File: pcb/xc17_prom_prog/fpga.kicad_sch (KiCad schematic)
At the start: 18 parts, among them J3 Conn_02x20_Odd_Even, U3 ICE40HX1K-VQ100

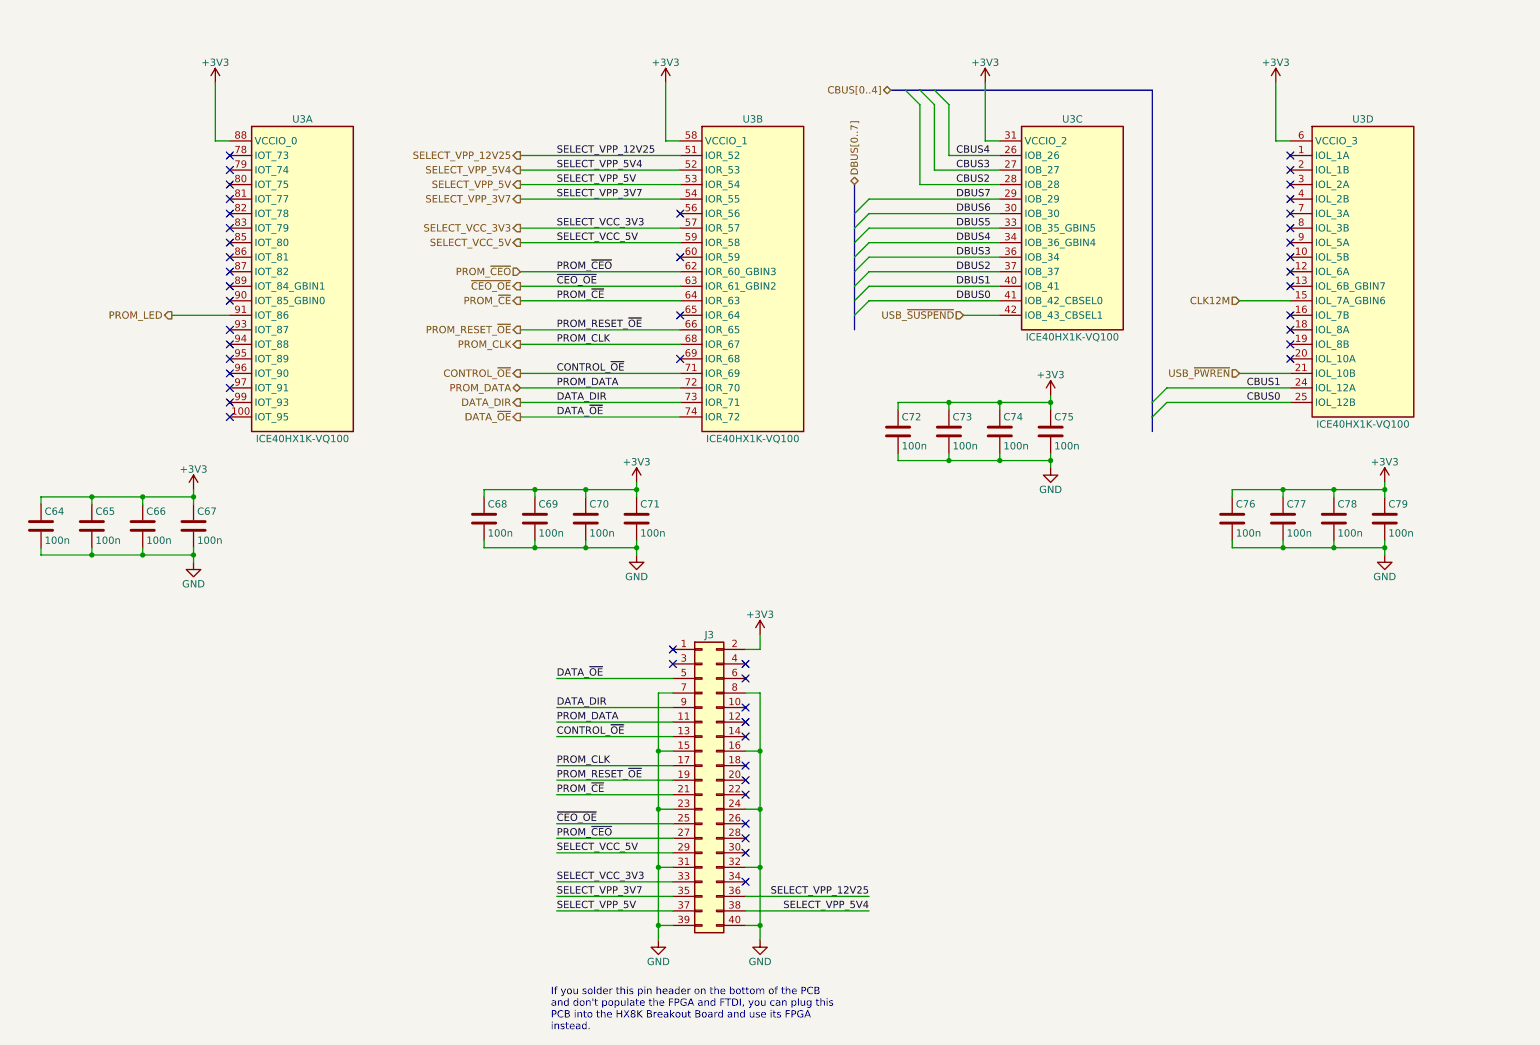
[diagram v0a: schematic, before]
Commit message: Fix MOSFETs
 * Block MOSFET body diodes by placing two MOSFETs in anti series.
 * Connect PROM LED to pin header.
 * Add transistors to actively pull PROM VCC and VPP low.
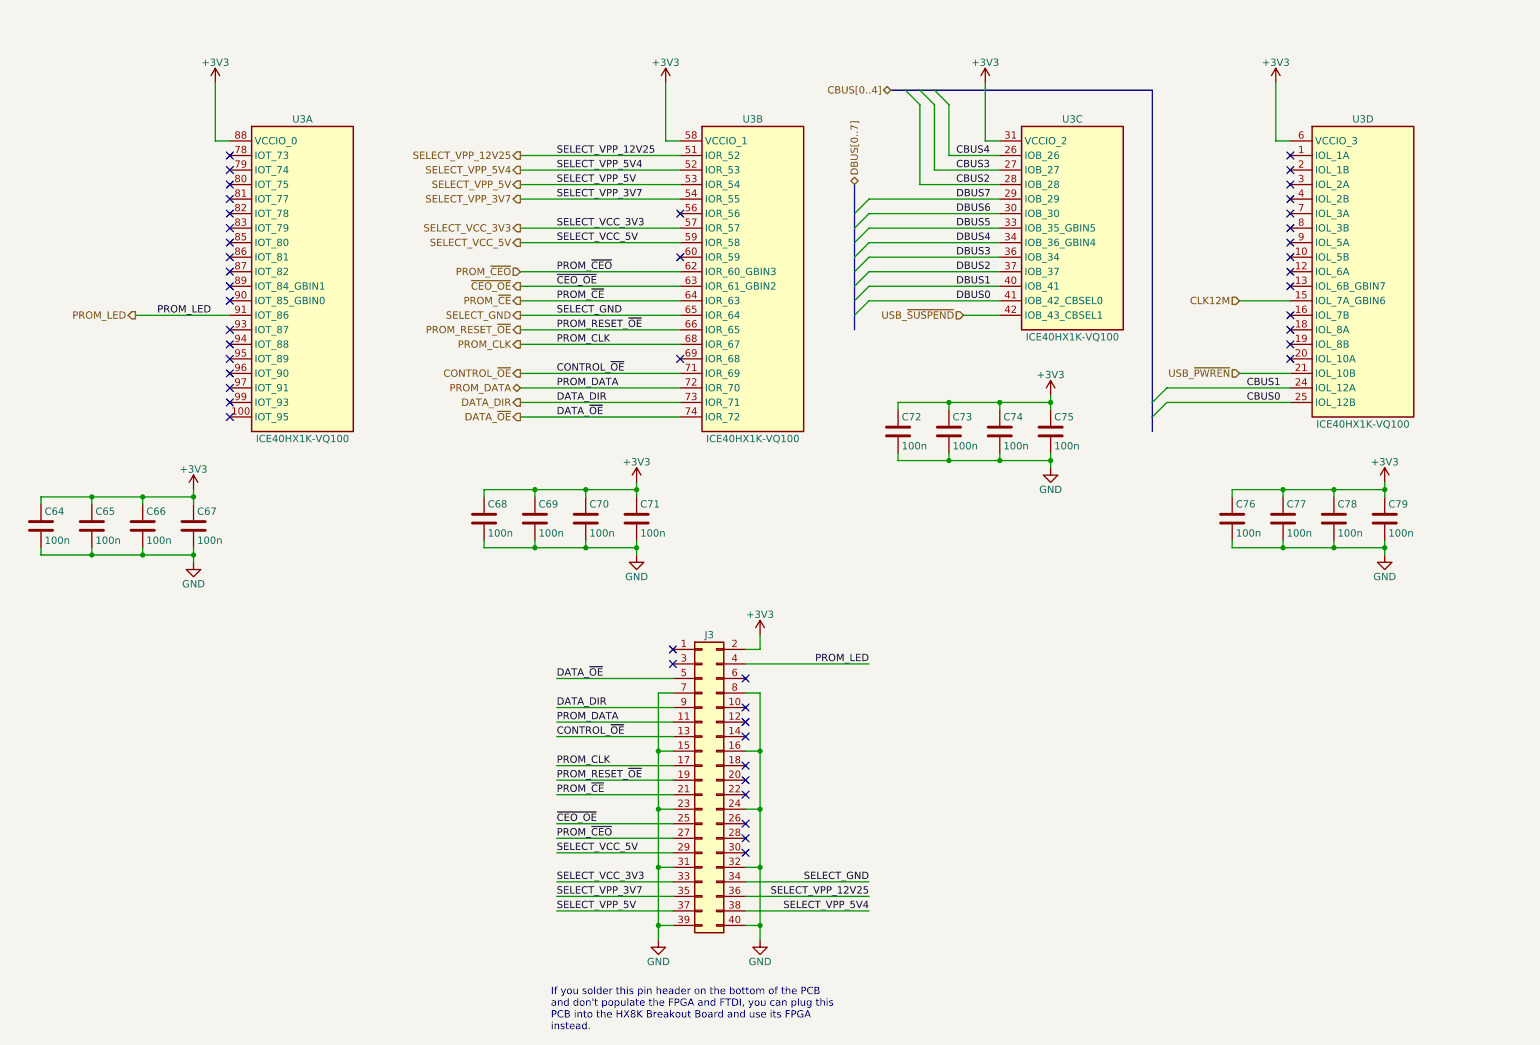
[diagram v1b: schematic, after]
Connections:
- net PROM_LED: now also J3.4 (Pin_4)
- net SELECT_GND: now reaches U3.65 (IOR_64)
- net SELECT_GND: now also J3.34 (Pin_34)
- no-connect marks 50 -> 47
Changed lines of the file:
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@@
 	(title_block
 		(title "XC17xxx PROM Programmer")
-		(date "2024-11-02")
-		(rev "0")
+		(date "2024-11-23")
+		(rev "1")
 		(company "CC-BY-SA-4.0 Michael Singer")
 		(comment 1 "https://github.com/msinger/xc17_prom_prog/")
@@
 	)
 	(no_connect
-		(at 144.78 167.64)
-	)
-	(no_connect
 		(at 144.78 137.16)
 	)
@@
 	)
 	(no_connect
-		(at 133.35 68.58)
-	)
-	(no_connect
 		(at 144.78 142.24)
 	)
 	(no_connect
-		(at 144.78 129.54)
-	)
-	(no_connect
 		(at 240.03 55.88)
 	)
@@
 	(wire
 		(pts
+			(xy 144.78 129.54) (xy 166.37 129.54)
+		)
+		(stroke
+			(width 0)
+			(type default)
+		)
+	)
+	(wire
+		(pts
 			(xy 99.06 107.95) (xy 99.06 109.22)
 		)
@@
 	(wire
 		(pts
-			(xy 44.45 68.58) (xy 54.61 68.58)
+			(xy 38.1 68.58) (xy 54.61 68.58)
 		)
 		(stroke
@@
 	(wire
 		(pts
+			(xy 105.41 68.58) (xy 133.35 68.58)
+		)
+		(stroke
+			(width 0)
+			(type default)
+		)
+	)
+	(wire
+		(pts
 			(xy 132.08 165.1) (xy 129.54 165.1)
 		)
@@
 	(wire
 		(pts
+			(xy 144.78 167.64) (xy 166.37 167.64)
+		)
+		(stroke
+			(width 0)
+			(type default)
+		)
+	)
+	(wire
+		(pts
 			(xy 99.06 109.22) (xy 107.95 109.22)
 		)
@@
 		)
 	)
+	(label "PROM_LED"
+		(at 41.91 68.58 0)
+		(fields_autoplaced yes)
+		(effects
+			(font
+				(size 1.27 1.27)
+			)
+			(justify left bottom)
+		)
+	)
 	(label "DATA_DIR"
 		(at 111.76 83.82 0)
@@
 		)
 	)
+	(label "SELECT_GND"
+		(at 166.37 167.64 180)
+		(fields_autoplaced yes)
+		(effects
+			(font
+				(size 1.27 1.27)
+			)
+			(justify right bottom)
+		)
+	)
 	(label "SELECT_VCC_3V3"
 		(at 111.76 167.64 0)
@@
 		)
 	)
+	(label "PROM_LED"
+		(at 166.37 129.54 180)
+		(fields_autoplaced yes)
+		(effects
+			(font
+				(size 1.27 1.27)
+			)
+			(justify right bottom)
+		)
+	)
 	(label "PROM_RESET_~{OE}"
 		(at 111.76 71.12 0)
@@
 		)
 	)
+	(label "SELECT_GND"
+		(at 111.76 68.58 0)
+		(fields_autoplaced yes)
+		(effects
+			(font
+				(size 1.27 1.27)
+			)
+			(justify left bottom)
+		)
+	)
 	(label "PROM_CLK"
 		(at 111.76 73.66 0)
@@
 		)
 	)
+	(hierarchical_label "SELECT_GND"
+		(shape output)
+		(at 105.41 68.58 180)
+		(fields_autoplaced yes)
+		(effects
+			(font
+				(size 1.27 1.27)
+			)
+			(justify right)
+		)
+	)
 	(hierarchical_label "SELECT_VCC_5V"
 		(shape output)
@@
 	(hierarchical_label "PROM_LED"
 		(shape output)
-		(at 44.45 68.58 180)
+		(at 38.1 68.58 180)
 		(fields_autoplaced yes)
 		(effects
@@
 		(on_board yes)
 		(dnp no)
-		(property "Reference" "#PWR0106"
+		(property "Reference" "#PWR0110"
 			(at 198.12 86.36 0)
 			(effects
@@
 			(project "xc17_prom_prog"
 				(path "/3afea672-343d-4fc8-b012-067ac21cc0e9/a8f52001-7a25-4283-bdf4-2dead0af6825"
-					(reference "#PWR0106")
+					(reference "#PWR0110")
 					(unit 1)
 				)
@@
 		(on_board yes)
 		(dnp no)
-		(property "Reference" "#PWR099"
+		(property "Reference" "#PWR0103"
 			(at 125.73 101.6 0)
 			(effects
@@
 			(project "xc17_prom_prog"
 				(path "/3afea672-343d-4fc8-b012-067ac21cc0e9/a8f52001-7a25-4283-bdf4-2dead0af6825"
-					(reference "#PWR099")
+					(reference "#PWR0103")
 					(unit 1)
 				)
@@
 		(on_board yes)
 		(dnp no)
-		(property "Reference" "#PWR097"
+		(property "Reference" "#PWR0101"
 			(at 48.26 118.11 0)
 			(effects
@@
 			(project "xc17_prom_prog"
 				(path "/3afea672-343d-4fc8-b012-067ac21cc0e9/a8f52001-7a25-4283-bdf4-2dead0af6825"
-					(reference "#PWR097")
+					(reference "#PWR0101")
 					(unit 1)
 				)
@@
 		(on_board yes)
 		(dnp no)
-		(property "Reference" "#PWR0104"
+		(property "Reference" "#PWR0108"
 			(at 147.32 184.15 0)
 			(effects
@@
 			(project ""
 				(path "/3afea672-343d-4fc8-b012-067ac21cc0e9/a8f52001-7a25-4283-bdf4-2dead0af6825"
-					(reference "#PWR0104")
+					(reference "#PWR0108")
 					(unit 1)
 				)
@@
 		(on_board yes)
 		(dnp no)
-		(property "Reference" "#PWR098"
+		(property "Reference" "#PWR0102"
 			(at 52.07 31.75 0)
 			(effects
@@
 			(project "xc17_prom_prog"
 				(path "/3afea672-343d-4fc8-b012-067ac21cc0e9/a8f52001-7a25-4283-bdf4-2dead0af6825"
-					(reference "#PWR098")
+					(reference "#PWR0102")
 					(unit 1)
 				)
@@
 		(on_board yes)
 		(dnp no)
-		(property "Reference" "#PWR0101"
+		(property "Reference" "#PWR0105"
 			(at 129.54 184.15 0)
 			(effects
@@
 			(project ""
 				(path "/3afea672-343d-4fc8-b012-067ac21cc0e9/a8f52001-7a25-4283-bdf4-2dead0af6825"
-					(reference "#PWR0101")
+					(reference "#PWR0105")
 					(unit 1)
 				)
@@
 		(on_board yes)
 		(dnp no)
-		(property "Reference" "#PWR0110"
+		(property "Reference" "#PWR0114"
 			(at 256.54 116.84 0)
 			(effects
@@
 			(project "xc17_prom_prog"
 				(path "/3afea672-343d-4fc8-b012-067ac21cc0e9/a8f52001-7a25-4283-bdf4-2dead0af6825"
-					(reference "#PWR0110")
+					(reference "#PWR0114")
 					(unit 1)
 				)
@@
 		(on_board yes)
 		(dnp no)
-		(property "Reference" "#PWR0100"
+		(property "Reference" "#PWR0104"
 			(at 125.73 116.84 0)
 			(effects
@@
 			(project "xc17_prom_prog"
 				(path "/3afea672-343d-4fc8-b012-067ac21cc0e9/a8f52001-7a25-4283-bdf4-2dead0af6825"
-					(reference "#PWR0100")
+					(reference "#PWR0104")
 					(unit 1)
 				)
@@
 		(on_board yes)
 		(dnp no)
-		(property "Reference" "#PWR0109"
+		(property "Reference" "#PWR0113"
 			(at 256.54 101.6 0)
 			(effects
@@
 			(project "xc17_prom_prog"
 				(path "/3afea672-343d-4fc8-b012-067ac21cc0e9/a8f52001-7a25-4283-bdf4-2dead0af6825"
-					(reference "#PWR0109")
+					(reference "#PWR0113")
 					(unit 1)
 				)
@@
 		(on_board yes)
 		(dnp no)
-		(property "Reference" "#PWR0103"
+		(property "Reference" "#PWR0107"
 			(at 147.32 128.27 0)
 			(effects
@@
 			(project ""
 				(path "/3afea672-343d-4fc8-b012-067ac21cc0e9/a8f52001-7a25-4283-bdf4-2dead0af6825"
-					(reference "#PWR0103")
+					(reference "#PWR0107")
 					(unit 1)
 				)
@@
 		(on_board yes)
 		(dnp no)
-		(property "Reference" "#PWR0105"
+		(property "Reference" "#PWR0109"
 			(at 186.69 31.75 0)
 			(effects
@@
 			(project "xc17_prom_prog"
 				(path "/3afea672-343d-4fc8-b012-067ac21cc0e9/a8f52001-7a25-4283-bdf4-2dead0af6825"
-					(reference "#PWR0105")
+					(reference "#PWR0109")
 					(unit 1)
 				)
@@
 		(on_board yes)
 		(dnp no)
-		(property "Reference" "#PWR0102"
+		(property "Reference" "#PWR0106"
 			(at 130.81 31.75 0)
 			(effects
@@
 			(project "xc17_prom_prog"
 				(path "/3afea672-343d-4fc8-b012-067ac21cc0e9/a8f52001-7a25-4283-bdf4-2dead0af6825"
-					(reference "#PWR0102")
+					(reference "#PWR0106")
 					(unit 1)
 				)
@@
 		(on_board yes)
 		(dnp no)
-		(property "Reference" "#PWR0108"
+		(property "Reference" "#PWR0112"
 			(at 237.49 31.75 0)
 			(effects
@@
 			(project "xc17_prom_prog"
 				(path "/3afea672-343d-4fc8-b012-067ac21cc0e9/a8f52001-7a25-4283-bdf4-2dead0af6825"
-					(reference "#PWR0108")
+					(reference "#PWR0112")
 					(unit 1)
 				)
@@
 		(on_board yes)
 		(dnp no)
-		(property "Reference" "#PWR0107"
+		(property "Reference" "#PWR0111"
 			(at 198.12 101.6 0)
 			(effects
@@
 			(project "xc17_prom_prog"
 				(path "/3afea672-343d-4fc8-b012-067ac21cc0e9/a8f52001-7a25-4283-bdf4-2dead0af6825"
-					(reference "#PWR0107")
+					(reference "#PWR0111")
 					(unit 1)
 				)
@@
 		(on_board yes)
 		(dnp no)
-		(property "Reference" "#PWR096"
+		(property "Reference" "#PWR0100"
 			(at 48.26 102.87 0)
 			(effects
@@
 			(project "xc17_prom_prog"
 				(path "/3afea672-343d-4fc8-b012-067ac21cc0e9/a8f52001-7a25-4283-bdf4-2dead0af6825"
-					(reference "#PWR096")
+					(reference "#PWR0100")
 					(unit 1)
 				)

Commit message: Implement more precise voltage controls
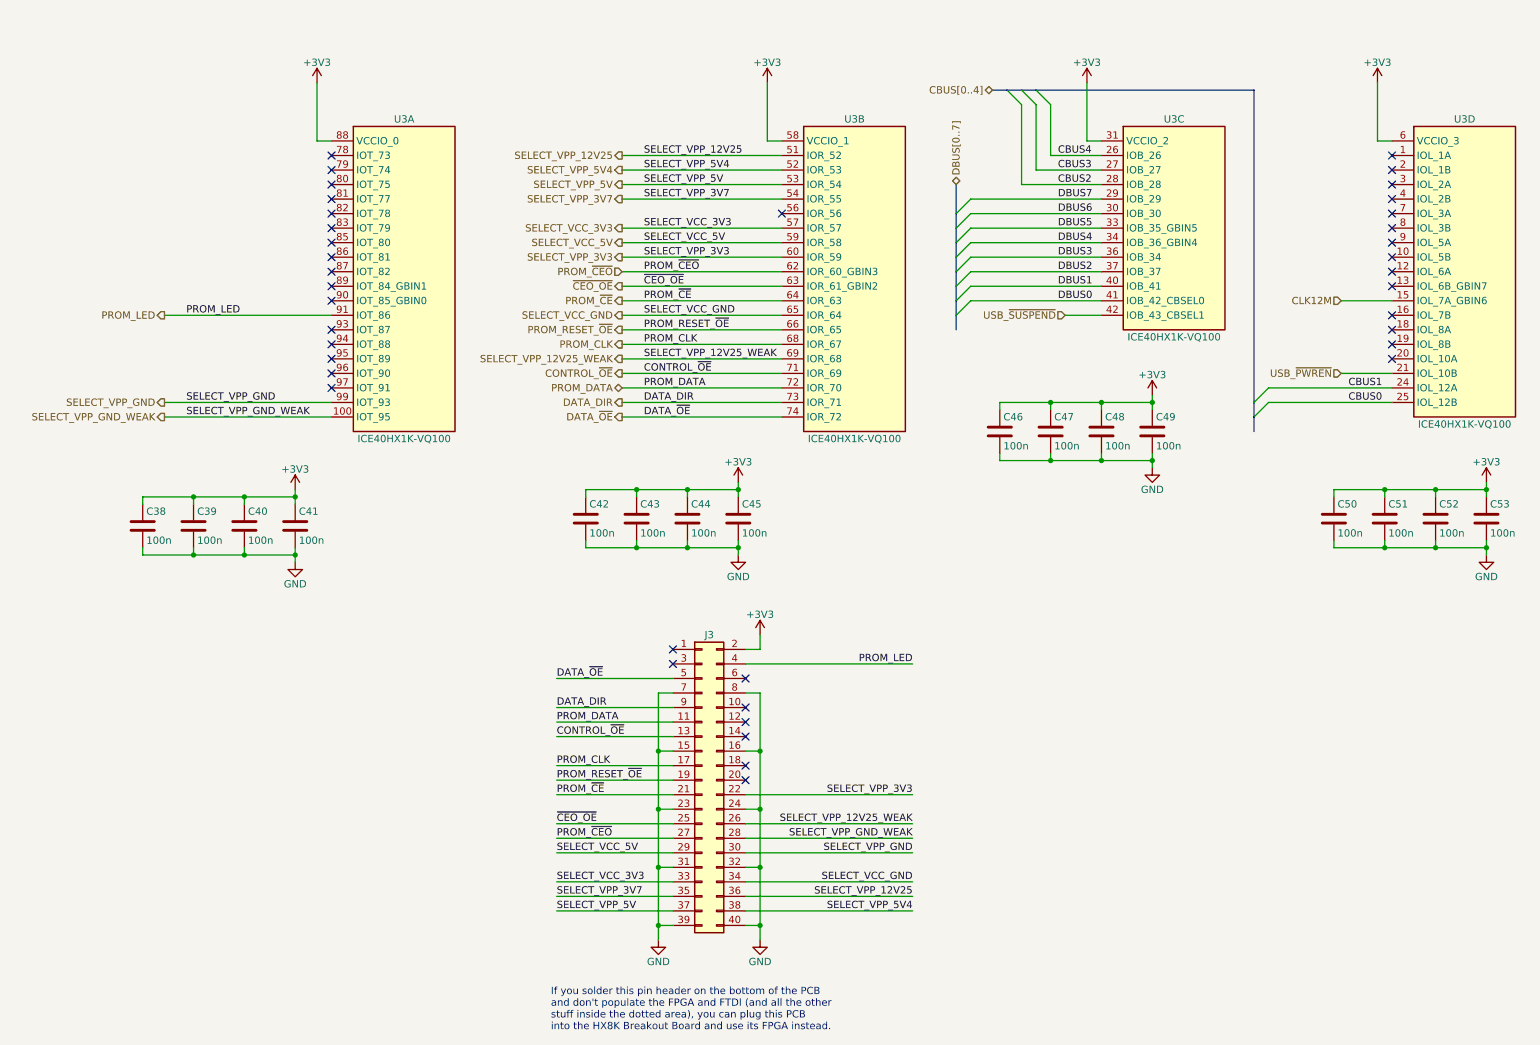
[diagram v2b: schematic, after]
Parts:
- renumbered C64 to C38, C65 to C39, C66 to C40, C67 to C41, C68 to C42, C69 to C43, C70 to C44, C71 to C45, C72 to C46, C73 to C47, C74 to C48, C75 to C49, C76 to C50, C77 to C51, C78 to C52, C79 to C53
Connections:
- net SELECT_VPP_GND_WEAK: now reaches U3.100 (IOT_95)
- net SELECT_VPP_GND_WEAK: now also J3.28 (Pin_28)
- net SELECT_VPP_GND: now reaches U3.99 (IOT_93)
- net SELECT_VPP_GND: now also J3.30 (Pin_30)
- net SELECT_VPP_3V3: now reaches U3.60 (IOR_59)
- net SELECT_VPP_3V3: now also J3.22 (Pin_22)
- net SELECT_VPP_12V25_WEAK: now reaches U3.69 (IOR_68)
- net SELECT_VPP_12V25_WEAK: now also J3.26 (Pin_26)
- net SELECT_GND renamed SELECT_VCC_GND
- no-connect marks 47 -> 39
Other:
- note added: "If you solder this pin header on the bottom of the PCB and don't populate the FPGA and FTDI (and all the other stuff inside the dotted area), you can plug this PCB into the HX8K Breakout Board and use its FPGA instead."
- note removed: "If you solder this pin header on the bottom of the PCB and don't populate the FPGA and FTDI, you can plug this PCB into the HX8K Breakout Board and use its FPGA instead."
- moved on the sheet: C38, C39, C40, C41, C42, C43, C44, C45, C46, C47, C48, C49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
